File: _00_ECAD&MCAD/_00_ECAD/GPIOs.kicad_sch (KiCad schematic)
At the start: 32 parts, among them K1 G5LE-1, K2 G5LE-1, Q1 MMBT5550L, Q2 MMBT5550L, Q3 MMBT5550L, Q4 MMBT5550L

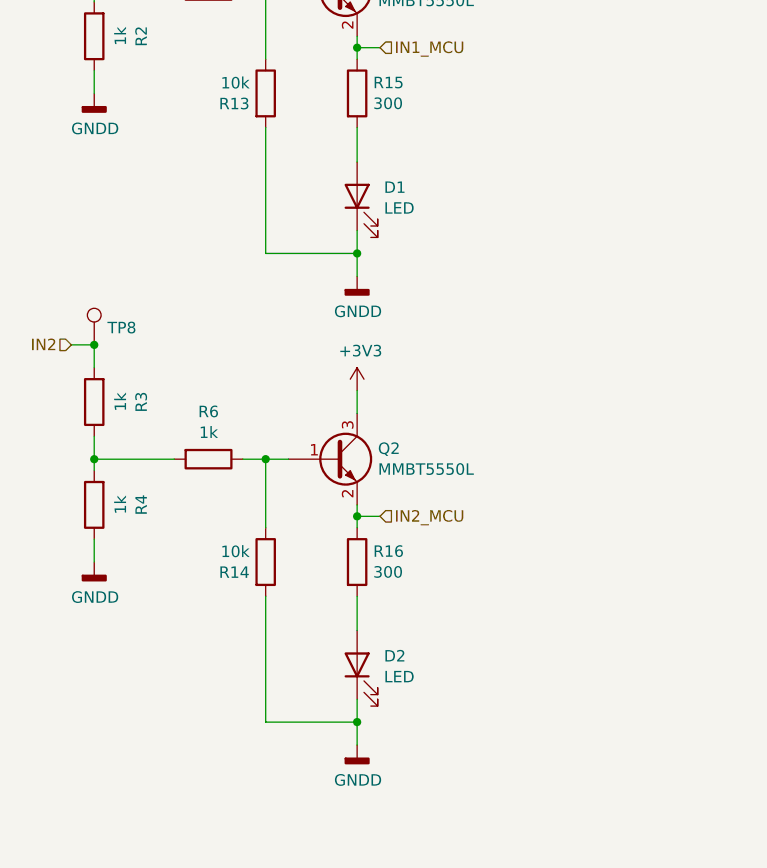
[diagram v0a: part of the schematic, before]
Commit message: Fix LED, common emitter issue, add adc feature
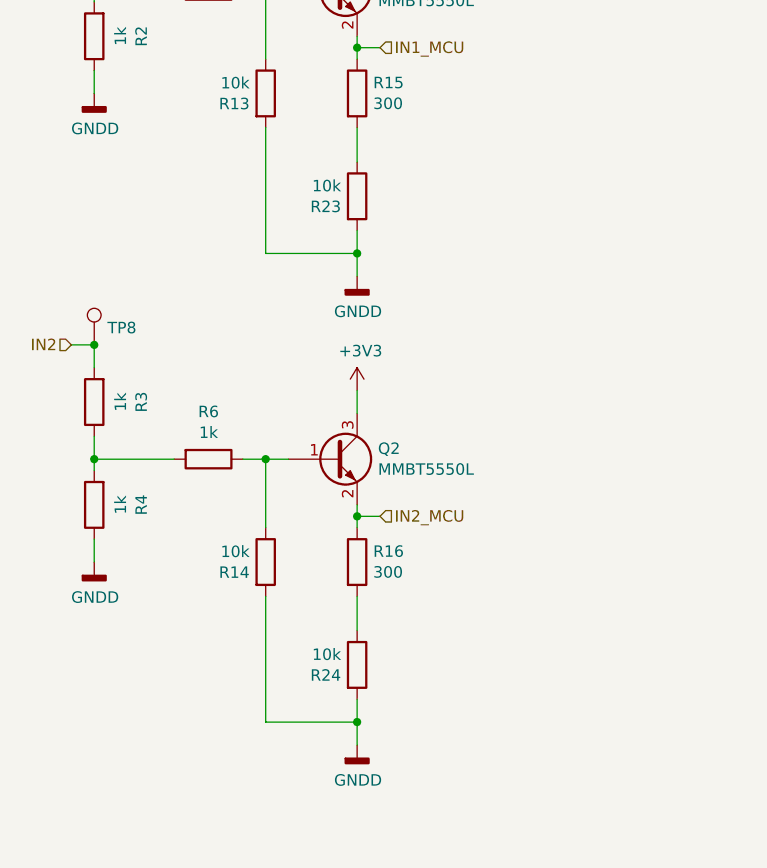
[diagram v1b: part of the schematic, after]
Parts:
- removed D1, D2: LED, LED_SMD:LED_1206_3216Metric_Pad1.42x1.75mm_HandSolder, symbol Device:LED
- added R23, R24: 10k, Resistor_SMD:R_1206_3216Metric_Pad1.30x1.75mm_HandSolder, symbol Device:R
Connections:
- net GNDD: now also R23.2, R24.2
- net at R15.2: now also R23.1
- net at R16.2: now also R24.1
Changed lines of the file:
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@@
     (pin "1")
-  )
-  (symbol (lib_id "Device:LED") (at 74.93 59.69 90) (unit 1)
-    (in_bom yes) (on_board yes)
-    (property "Reference" "D1" (id 0) (at 77.9018 58.7248 90)
-      (effects (font (size 1.27 1.27)) (justify right))
-    )
-    (property "Value" "LED" (id 1) (at 77.9018 61.0362 90)
-      (effects (font (size 1.27 1.27)) (justify right))
-    )
-    (property "Footprint" "LED_SMD:LED_1206_3216Metric_Pad1.42x1.75mm_HandSolder" (id 2) (at 74.93 59.69 0)
-      (effects (font (size 1.27 1.27)) hide)
-    )
-    (property "Datasheet" "~" (id 3) (at 74.93 59.69 0)
-      (effects (font (size 1.27 1.27)) hide)
-    )
-    (pin "1")
-    (pin "2")
   )
   (symbol (lib_id "Device:R") (at 45.72 30.48 180) (unit 1)
@@
     )
     (pin "1")
-  )
-  (symbol (lib_id "Device:LED") (at 74.93 111.76 90) (unit 1)
-    (in_bom yes) (on_board yes)
-    (property "Reference" "D2" (id 0) (at 77.9018 110.7948 90)
-      (effects (font (size 1.27 1.27)) (justify right))
-    )
-    (property "Value" "LED" (id 1) (at 77.9018 113.1062 90)
-      (effects (font (size 1.27 1.27)) (justify right))
-    )
-    (property "Footprint" "LED_SMD:LED_1206_3216Metric_Pad1.42x1.75mm_HandSolder" (id 2) (at 74.93 111.76 0)
-      (effects (font (size 1.27 1.27)) hide)
-    )
-    (property "Datasheet" "~" (id 3) (at 74.93 111.76 0)
-      (effects (font (size 1.27 1.27)) hide)
-    )
-    (pin "1")
-    (pin "2")
   )
   (symbol (lib_id "Device:R") (at 45.72 82.55 180) (unit 1)
@@
     (pin "5")
   )
+  (symbol (lib_id "Device:R") (at 74.93 111.76 0) (unit 1)
+    (in_bom yes) (on_board yes)
+    (property "Reference" "R24" (id 0) (at 73.152 112.9284 0)
+      (effects (font (size 1.27 1.27)) (justify right))
+    )
+    (property "Value" "10k" (id 1) (at 73.152 110.617 0)
+      (effects (font (size 1.27 1.27)) (justify right))
+    )
+    (property "Footprint" "Resistor_SMD:R_1206_3216Metric_Pad1.30x1.75mm_HandSolder" (id 2) (at 73.152 111.76 90)
+      (effects (font (size 1.27 1.27)) hide)
+    )
+    (property "Datasheet" "~" (id 3) (at 74.93 111.76 0)
+      (effects (font (size 1.27 1.27)) hide)
+    )
+    (pin "1")
+    (pin "2")
+  )
+  (symbol (lib_id "Device:R") (at 74.93 59.69 0) (unit 1)
+    (in_bom yes) (on_board yes)
+    (property "Reference" "R23" (id 0) (at 73.152 60.8584 0)
+      (effects (font (size 1.27 1.27)) (justify right))
+    )
+    (property "Value" "10k" (id 1) (at 73.152 58.547 0)
+      (effects (font (size 1.27 1.27)) (justify right))
+    )
+    (property "Footprint" "Resistor_SMD:R_1206_3216Metric_Pad1.30x1.75mm_HandSolder" (id 2) (at 73.152 59.69 90)
+      (effects (font (size 1.27 1.27)) hide)
+    )
+    (property "Datasheet" "~" (id 3) (at 74.93 59.69 0)
+      (effects (font (size 1.27 1.27)) hide)
+    )
+    (pin "1")
+    (pin "2")
+  )
 )
